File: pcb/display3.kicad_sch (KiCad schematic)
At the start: 35 parts, among them Q25 2N7002K, Q26 2N7002K, Q27 2N7002K, Q28 2N7002K, Q29 BSS84, Q30 BSS84, Q31 BSS84, Q32 BSS84, Q33 BSS84, Q34 BSS84, Q35 BSS84, Q36 BSS84, U4 74HC595

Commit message: tentative schematic for common cathode
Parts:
- C8: renamed from C6; footprint (none) -> Capacitor_SMD:C_0805_2012Metric_Pad1.18x1.45mm_HandSolder
- R48: renamed from R45; footprint Resistor_SMD:R_0805_2012Metric_Pad1.15x1.40mm_HandSolder -> Resistor_SMD:R_0805_2012Metric_Pad1.20x1.40mm_HandSolder
- R49: renamed from R46; footprint Resistor_SMD:R_0805_2012Metric_Pad1.15x1.40mm_HandSolder -> Resistor_SMD:R_0805_2012Metric_Pad1.20x1.40mm_HandSolder
- R50: renamed from R47; footprint Resistor_SMD:R_0805_2012Metric_Pad1.15x1.40mm_HandSolder -> Resistor_SMD:R_0805_2012Metric_Pad1.20x1.40mm_HandSolder
- R51: renamed from R48; footprint Resistor_SMD:R_0805_2012Metric_Pad1.15x1.40mm_HandSolder -> Resistor_SMD:R_0805_2012Metric_Pad1.20x1.40mm_HandSolder
- R52: renamed from R49; footprint Resistor_SMD:R_0805_2012Metric_Pad1.15x1.40mm_HandSolder -> Resistor_SMD:R_0805_2012Metric_Pad1.20x1.40mm_HandSolder
- R53: renamed from R50; footprint Resistor_SMD:R_0805_2012Metric_Pad1.15x1.40mm_HandSolder -> Resistor_SMD:R_0805_2012Metric_Pad1.20x1.40mm_HandSolder
- R54: renamed from R51; footprint Resistor_SMD:R_0805_2012Metric_Pad1.15x1.40mm_HandSolder -> Resistor_SMD:R_0805_2012Metric_Pad1.20x1.40mm_HandSolder
- R55: renamed from R52; footprint Resistor_SMD:R_0805_2012Metric_Pad1.15x1.40mm_HandSolder -> Resistor_SMD:R_0805_2012Metric_Pad1.20x1.40mm_HandSolder
- R56: renamed from R53; footprint (none) -> Resistor_SMD:R_0805_2012Metric_Pad1.20x1.40mm_HandSolder
- R57: renamed from R54; footprint (none) -> Resistor_SMD:R_0805_2012Metric_Pad1.20x1.40mm_HandSolder
- R58: renamed from R55; footprint (none) -> Resistor_SMD:R_0805_2012Metric_Pad1.20x1.40mm_HandSolder
- R59: renamed from R56; footprint (none) -> Resistor_SMD:R_0805_2012Metric_Pad1.20x1.40mm_HandSolder
- R60: renamed from R57; footprint Resistor_SMD:R_0805_2012Metric_Pad1.15x1.40mm_HandSolder -> Resistor_SMD:R_0805_2012Metric_Pad1.20x1.40mm_HandSolder
- R61: renamed from R58; footprint Resistor_SMD:R_0805_2012Metric_Pad1.15x1.40mm_HandSolder -> Resistor_SMD:R_0805_2012Metric_Pad1.20x1.40mm_HandSolder
- R62: renamed from R59; footprint Resistor_SMD:R_0805_2012Metric_Pad1.15x1.40mm_HandSolder -> Resistor_SMD:R_0805_2012Metric_Pad1.20x1.40mm_HandSolder
- R63: renamed from R62; footprint Resistor_SMD:R_0805_2012Metric_Pad1.15x1.40mm_HandSolder -> Resistor_SMD:R_0805_2012Metric_Pad1.20x1.40mm_HandSolder
- R64: renamed from R63; footprint (none) -> Resistor_SMD:R_0805_2012Metric_Pad1.20x1.40mm_HandSolder
- R65: renamed from R64; footprint (none) -> Resistor_SMD:R_0805_2012Metric_Pad1.20x1.40mm_HandSolder
- R66: renamed from R65; footprint (none) -> Resistor_SMD:R_0805_2012Metric_Pad1.20x1.40mm_HandSolder
- R67: renamed from R66; footprint (none) -> Resistor_SMD:R_0805_2012Metric_Pad1.20x1.40mm_HandSolder
- renumbered D3 to D4

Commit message: common anode schematic
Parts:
- removed C8: 0.1uF, Capacitor_SMD:C_0805_2012Metric_Pad1.18x1.45mm_HandSolder, symbol Device:C_Small
- removed D4: KW4-S561CAB YELLOW SMD, mtg_life_counter:KW4-S561xxB_SMD, symbol mtg_life_counter:KW4-S561CxB
- removed Q25, Q26, Q27, Q28: 2N7002K, Package_TO_SOT_SMD:SOT-23, symbol Transistor_FET:2N7002K
- removed Q29, Q30, Q31, Q32, Q33, Q34, Q35, Q36: BSS84, Package_TO_SOT_SMD:SOT-23, symbol Transistor_FET:BSS84
- removed R48, R49, R50, R51, R52, R53, R54, R55, R56, R57, R58, R59, R60, R61, R62, R63, R64, R65, R66, R67: 330R, Resistor_SMD:R_0805_2012Metric_Pad1.20x1.40mm_HandSolder, symbol Device:R
- removed U4: 74HC595, Package_SO:SOIC-16_3.9x9.9mm_P1.27mm, symbol 74xx:74HC595
- added D4: KW4-S561AAB, mtg_life_counter:KW4-S561xxB_SMD, symbol mtg_life_counter:KW4-S561AxB
- added Q10, Q11, Q12, Q9: DMG2301L, Package_TO_SOT_SMD:SOT-23, symbol Transistor_FET:DMG2301L
- added R34, R35, R36, R37, R38, R39, R40, R41, R42, R43, R44, R45: 330R, Resistor_SMD:R_0805_2012Metric_Pad1.20x1.40mm_HandSolder, symbol Device:R
- added R46: 10k, Resistor_SMD:R_0805_2012Metric_Pad1.20x1.40mm_HandSolder, symbol Device:R
- added U4: TPIC6C596, Package_SO:SOIC-16_3.9x9.9mm_P1.27mm, symbol mtg_life_counter:TPIC6C596
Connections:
- net +5V: now also Q10.3 (D), Q11.3 (D), Q12.3 (D), Q9.3 (D), R46.1, U4.1 (VCC)
- net DIGIT_SEL_1: now also R34.1
- net DIGIT_SEL_2: now also R35.1
- net DIGIT_SEL_3: now also R36.1
- net DIGIT_SEL_4: now also R37.1
- net GND: now also U4.16 (GND), U4.8 (~{G})
- net SHIFT_CLK: now also U4.15 (SRCK)
- net SHIFT_IN: now also U4.2 (SER_IN)
- net SHIFT_LATCH: now also U4.10 (RCLK)
- net SHIFT_OUT: now also U4.9 (SER_OUT)
- new net: Q9.1 (G), R34.2
- new net: Q12.1 (G), R37.2
- new net: Q11.1 (G), R36.2
- new net: Q10.1 (G), R35.2
- new net: R46.2, U4.7 (~{SRCLR})
- new net AA: D4.11 (a), R38.1
- new net AB: D4.7 (b), R39.1
- new net AC: D4.4 (c), R40.1
- new net AD: D4.2 (d), R41.1
- new net ADP: D4.3 (DP), R45.1
- new net AE: D4.1 (e), R42.1
- new net AF: D4.10 (f), R43.1
- new net AG: D4.5 (g), R44.1
- new net CA1: D4.12 (CA1), Q9.2 (S)
- new net CA2: D4.9 (CA2), Q10.2 (S)
- new net CA3: D4.8 (CA3), Q11.2 (S)
- new net CA4: D4.6 (CA4), Q12.2 (S)
- new net SA: R38.2, U4.3 (DRAIN0)
- new net SB: R39.2, U4.4 (DRAIN1)
- new net SC: R40.2, U4.5 (DRAIN2)
- new net SD: R41.2, U4.6 (DRAIN3)
- new net SDP: R45.2, U4.14 (DRAIN7)
- new net SE: R42.2, U4.11 (DRAIN4)
- new net SF: R43.2, U4.12 (DRAIN5)
- new net SG: R44.2, U4.13 (DRAIN6)

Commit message: continue wip
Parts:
- added C8: 0.1uF, Capacitor_SMD:C_0805_2012Metric_Pad1.18x1.45mm_HandSolder, symbol Device:C_Small
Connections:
- net +5V: now also C8.1
- net GND: now also C8.2
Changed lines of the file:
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@@
+	(wire
+		(pts
+			(xy 200.66 58.42) (xy 200.66 60.96)
+		)
+		(stroke
+			(width 0)
+			(type default)
+		)
+	)
 	(wire
 		(pts
@@
 		(pts
 			(xy 190.5 73.66) (xy 198.12 73.66)
+		)
+		(stroke
+			(width 0)
+			(type default)
+		)
+	)
+	(wire
+		(pts
+			(xy 200.66 50.8) (xy 200.66 53.34)
 		)
 		(stroke
@@
 	)
 	(symbol
+		(lib_id "Device:C_Small")
+		(at 200.66 55.88 0)
+		(mirror y)
+		(unit 1)
+		(exclude_from_sim no)
+		(in_bom yes)
+		(on_board yes)
+		(dnp no)
+		(fields_autoplaced yes)
+		(property "Reference" "C8"
+			(at 203.2 54.6162 0)
+			(effects
+				(font
+					(size 1.27 1.27)
+				)
+				(justify right)
+			)
+		)
+		(property "Value" "0.1uF"
+			(at 203.2 57.1562 0)
+			(effects
+				(font
+					(size 1.27 1.27)
+				)
+				(justify right)
+			)
+		)
+		(property "Footprint" "Capacitor_SMD:C_0805_2012Metric_Pad1.18x1.45mm_HandSolder"
+			(at 200.66 55.88 0)
+			(effects
+				(font
+					(size 1.27 1.27)
+				)
+				(hide yes)
+			)
+		)
+		(property "Datasheet" "~"
+			(at 200.66 55.88 0)
+			(effects
+				(font
+					(size 1.27 1.27)
+				)
+				(hide yes)
+			)
+		)
+		(property "Description" "Unpolarized capacitor, small symbol"
+			(at 200.66 55.88 0)
+			(effects
+				(font
+					(size 1.27 1.27)
+				)
+				(hide yes)
+			)
+		)
+		(pin "2"
+		)
+		(pin "1"
+		)
+		(instances
+			(project "mtg_life_counter"
+				(path "/1883df74-0bd5-446c-9076-f848bb3cfebf/9592e857-eda4-4ed1-a70a-bb63f68d12f3"
+					(reference "C8")
+					(unit 1)
+				)
+			)
+		)
+	)
+	(symbol
 		(lib_id "Transistor_FET:DMG2301L")
 		(at 60.96 33.02 0)
@@
 					(unit 1)
 				)
+			)
+		)
+	)
+	(symbol
+		(lib_id "power:GND")
+		(at 200.66 60.96 0)
+		(unit 1)
+		(exclude_from_sim no)
+		(in_bom yes)
+		(on_board yes)
+		(dnp no)
+		(property "Reference" "#PWR068"
+			(at 200.66 67.31 0)
+			(effects
+				(font
+					(size 1.27 1.27)
+				)
+				(hide yes)
+			)
+		)
+		(property "Value" "GND"
+			(at 200.66 64.77 0)
+			(effects
+				(font
+					(size 1.27 1.27)
+				)
+			)
+		)
+		(property "Footprint" ""
+			(at 200.66 60.96 0)
+			(effects
+				(font
+					(size 1.27 1.27)
+				)
+				(hide yes)
+			)
+		)
+		(property "Datasheet" ""
+			(at 200.66 60.96 0)
+			(effects
+				(font
+					(size 1.27 1.27)
+				)
+				(hide yes)
+			)
+		)
+		(property "Description" "Power symbol creates a global label with name \"GND\" , ground"
+			(at 200.66 60.96 0)
+			(effects
+				(font
+					(size 1.27 1.27)
+				)
+				(hide yes)
+			)
+		)
+		(pin "1"
+		)
+		(instances
+			(project "mtg_life_counter"
+				(path "/1883df74-0bd5-446c-9076-f848bb3cfebf/9592e857-eda4-4ed1-a70a-bb63f68d12f3"
+					(reference "#PWR068")
+					(unit 1)
+				)
+			)
+		)
+	)
+	(symbol
+		(lib_id "power:+5V")
+		(at 200.66 50.8 0)
+		(unit 1)
+		(exclude_from_sim no)
+		(in_bom yes)
+		(on_board yes)
+		(dnp no)
+		(property "Reference" "#PWR067"
+			(at 200.66 54.61 0)
+			(effects
+				(font
+					(size 1.27 1.27)
+				)
+				(hide yes)
+			)
+		)
+		(property "Value" "+5V"
+			(at 200.66 46.99 0)
+			(effects
+				(font
+					(size 1.27 1.27)
+				)
+			)
+		)
+		(property "Footprint" ""
+			(at 200.66 50.8 0)
+			(effects
+				(font
+					(size 1.27 1.27)
+				)
+				(hide yes)
+			)
+		)
+		(property "Datasheet" ""
+			(at 200.66 50.8 0)
+			(effects
+				(font
+					(size 1.27 1.27)
+				)
+				(hide yes)
+			)
+		)
+		(property "Description" "Power symbol creates a global label with name \"+5V\""
+			(at 200.66 50.8 0)
+			(effects
+				(font
+					(size 1.27 1.27)
+				)
+				(hide yes)
+			)
+		)
+		(pin "1"
+		)
+		(instances
+			(project "mtg_life_counter"
+				(path "/1883df74-0bd5-446c-9076-f848bb3cfebf/9592e857-eda4-4ed1-a70a-bb63f68d12f3"
+					(reference "#PWR067")
+					(unit 1)
+				)

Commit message: start to route display traces
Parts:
- removed R46: 10k, Resistor_SMD:R_0805_2012Metric_Pad1.20x1.40mm_HandSolder, symbol Device:R
- renumbered D4 to D3, R34 to R32, R35 to R33, R36 to R34, R37 to R35, R38 to R36, R39 to R37, R40 to R38, R41 to R39, R42 to R40, R43 to R41, R44 to R42, R45 to R43
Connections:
- net +5V: now also U4.7 (~{SRCLR})

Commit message: continue layout. improve 3d model
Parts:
- D3: footprint mtg_life_counter:KW4-S561xxB_SMD -> mtg_life_counter:KW4-S561xAB_SMD
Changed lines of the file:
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@@
 			)
 		)
-		(property "Footprint" "mtg_life_counter:KW4-S561xxB_SMD"
+		(property "Footprint" "mtg_life_counter:KW4-S561xAB_SMD"
 			(at 132.08 95.25 0)
 			(effects

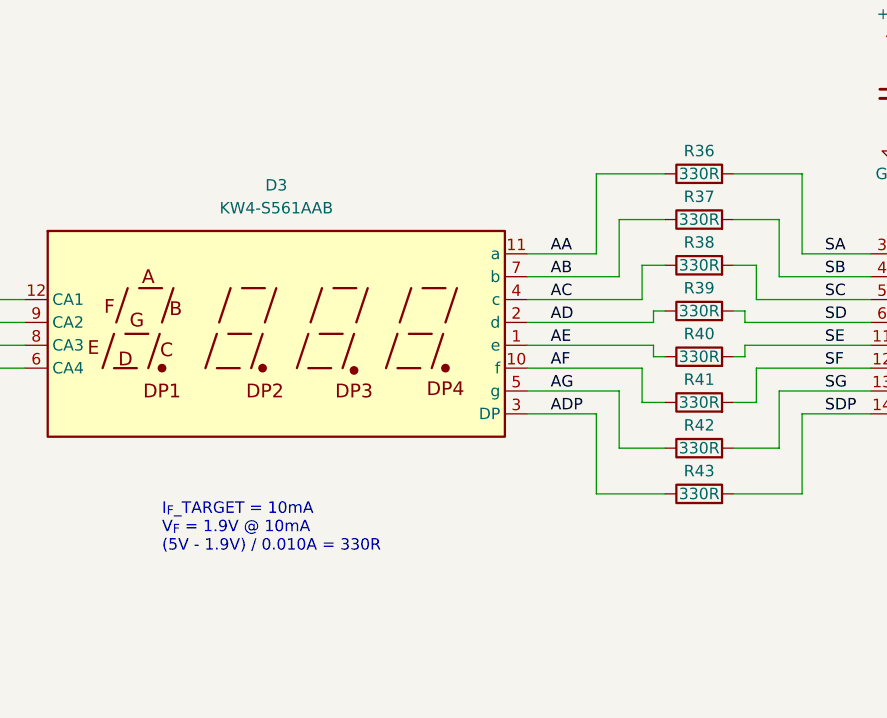
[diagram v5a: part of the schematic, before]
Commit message: continue layout. update leds for KD4 led modules
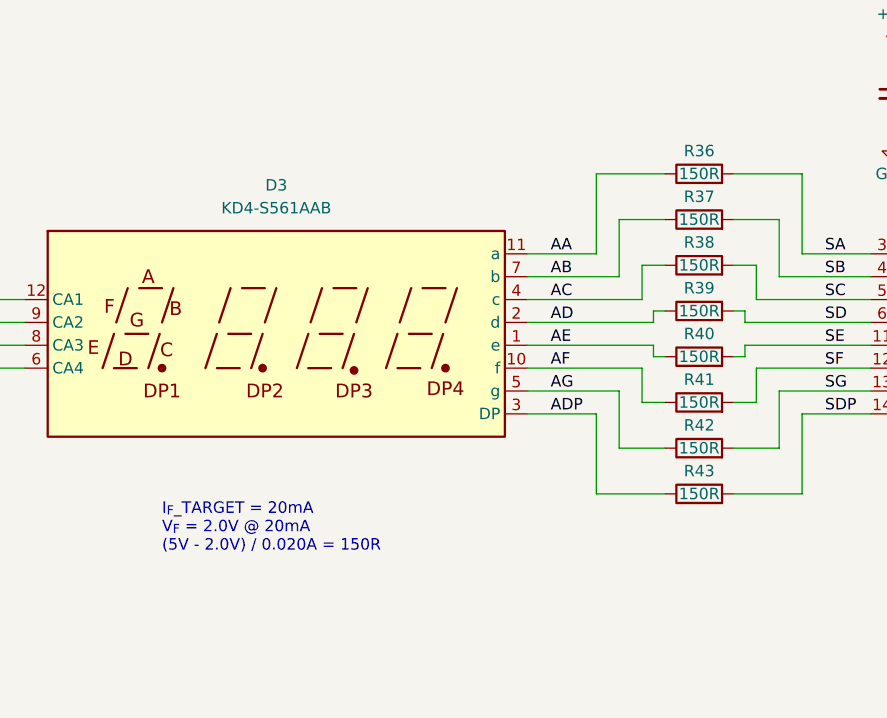
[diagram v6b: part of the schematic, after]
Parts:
- D3: value KW4-S561AAB -> KD4-S561AAB; footprint mtg_life_counter:KW4-S561xAB_SMD -> mtg_life_counter:KD4-S561xxB_SMD_Slim
- R36, R37, R38, R39, R40, R41, R42, R43: value 330R -> 150R
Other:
- note added: "I_{F}_TARGET = 20mA V_{F} = 2.0V @ 20mA (5V - 2.0V) / 0.020A = 150R"
- note removed: "I_{F}_TARGET = 10mA V_{F} = 1.9V @ 10mA (5V - 1.9V) / 0.010A = 330R"
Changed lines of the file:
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@@
 		(company "Max Proskauer")
 	)
-	(text "I_{F}_TARGET = 10mA\nV_{F} = 1.9V @ 10mA\n(5V - 1.9V) / 0.010A = 330R"
+	(text "I_{F}_TARGET = 20mA\nV_{F} = 2.0V @ 20mA\n(5V - 2.0V) / 0.020A = 150R"
 		(exclude_from_sim no)
 		(at 119.38 104.14 0)
@@
 			)
 		)
-		(property "Value" "330R"
+		(property "Value" "150R"
 			(at 179.07 64.77 90)
 			(effects
@@
 			)
 		)
-		(property "Value" "330R"
+		(property "Value" "150R"
 			(at 179.07 80.01 90)
 			(effects
@@
 			)
 		)
-		(property "Value" "330R"
+		(property "Value" "150R"
 			(at 179.07 100.33 90)
 			(effects
@@
 			)
 		)
-		(property "Value" "330R"
+		(property "Value" "150R"
 			(at 179.07 95.25 90)
 			(effects
@@
 			)
 		)
-		(property "Value" "330R"
+		(property "Value" "150R"
 			(at 179.07 74.93 90)
 			(effects
@@
 			)
 		)
-		(property "Value" "330R"
+		(property "Value" "150R"
 			(at 179.07 85.09 90)
 			(effects
@@
 			)
 		)
-		(property "Value" "330R"
+		(property "Value" "150R"
 			(at 179.07 69.85 90)
 			(effects
@@
 			)
 		)
-		(property "Value" "330R"
+		(property "Value" "150R"
 			(at 179.07 90.17 90)
 			(effects
@@
 			)
 		)
-		(property "Value" "KW4-S561AAB"
+		(property "Value" "KD4-S561AAB"
 			(at 132.08 68.58 0)
 			(effects
@@
 			)
 		)
-		(property "Footprint" "mtg_life_counter:KW4-S561xAB_SMD"
+		(property "Footprint" "mtg_life_counter:KD4-S561xxB_SMD_Slim"
 			(at 132.08 95.25 0)
 			(effects
